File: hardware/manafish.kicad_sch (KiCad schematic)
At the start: 9 parts, among them J12 Magnet, J6 Battery, J8 USB_C_Receptacle_USB2.0_14P

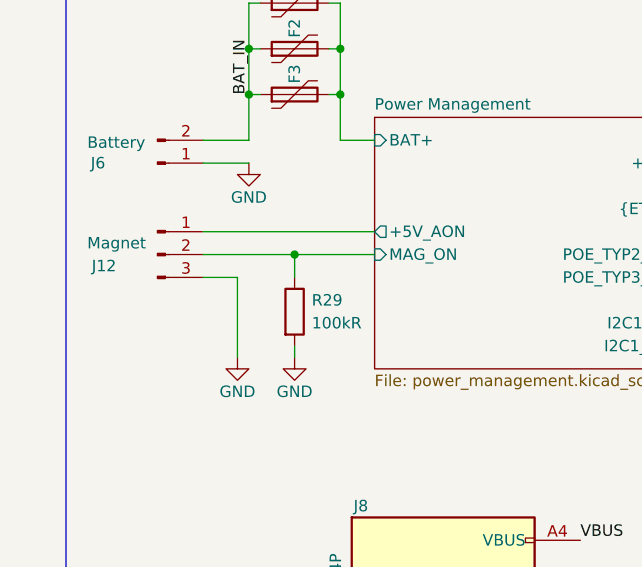
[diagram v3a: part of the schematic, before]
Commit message: Separate the supply pins on breakout headers J9 and J13
Both headers now start with +5V, GND, GND, +3.3V (pins 1-4), so 5 V
and 3.3 V only meet diagonally and each supply pin has GND beside it.
The GPIOs that sat on pins 3/4 moved to the end of each header.

Co-Authored-By: Claude Opus 5.5 <noreply@anthropic.com>
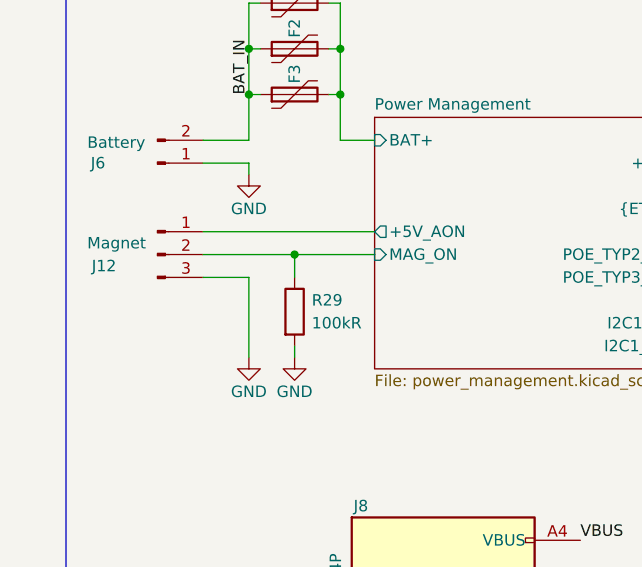
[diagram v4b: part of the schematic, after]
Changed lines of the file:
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@@
 	(wire
 		(pts
+			(xy 35.56 43.18) (xy 35.56 41.91)
+		)
+		(stroke
+			(width 0)
+			(type default)
+		)
+	)
+	(wire
+		(pts
 			(xy 181.61 95.25) (xy 184.15 95.25)
 		)
@@
 		)
 	)
+	(wire
+		(pts
+			(xy 35.56 41.91) (xy 30.48 41.91)
+		)
+		(stroke
+			(width 0)
+			(type default)
+		)
+	)
 	(bus
 		(pts
@@
 	(wire
 		(pts
-			(xy 34.29 54.61) (xy 30.48 54.61)
+			(xy 35.56 54.61) (xy 30.48 54.61)
 		)
 		(stroke
@@
 	(wire
 		(pts
-			(xy 34.29 54.61) (xy 34.29 63.5)
+			(xy 35.56 54.61) (xy 35.56 63.5)
 		)
 		(stroke
@@
 	)
 	(symbol
+		(lib_id "power:GND")
+		(at 35.56 43.18 0)
+		(unit 1)
+		(body_style 1)
+		(exclude_from_sim no)
+		(in_bom no)
+		(on_board no)
+		(in_pos_files no)
+		(dnp no)
+		(property "Reference" "#PWR0175"
+			(at 35.56 49.53 0)
+			(hide yes)
+			(show_name no)
+			(do_not_autoplace no)
+			(effects
+				(font
+					(size 1.27 1.27)
+				)
+			)
+		)
+		(property "Value" "GND"
+			(at 35.56 46.99 0)
+			(show_name no)
+			(do_not_autoplace no)
+			(effects
+				(font
+					(size 1.27 1.27)
+				)
+			)
+		)
+		(property "Footprint" ""
+			(at 35.56 43.18 0)
+			(hide yes)
+			(show_name no)
+			(do_not_autoplace no)
+			(effects
+				(font
+					(size 1.27 1.27)
+				)
+			)
+		)
+		(property "Datasheet" ""
+			(at 35.56 43.18 0)
+			(hide yes)
+			(show_name no)
+			(do_not_autoplace no)
+			(effects
+				(font
+					(size 1.27 1.27)
+				)
+			)
+		)
+		(property "Description" "Power symbol creates a global label with name \"GND\" , ground"
+			(at 35.56 43.18 0)
+			(hide yes)
+			(show_name no)
+			(do_not_autoplace no)
+			(effects
+				(font
+					(size 1.27 1.27)
+				)
+			)
+		)
+		(pin "1"
+		)
+		(instances
+			(project "manafish"
+				(path "/37283e3e-a087-4659-9b29-171eab26a1f6"
+					(reference "#PWR0175")
+					(unit 1)
+				)
+			)
+		)
+	)
+	(symbol
 		(lib_id "Connector:Conn_01x02_Pin")
 		(at 25.4 41.91 0)
@@
 	(symbol
 		(lib_id "power:GND")
-		(at 34.29 63.5 0)
+		(at 35.56 63.5 0)
 		(unit 1)
 		(body_style 1)
@@
 		(dnp no)
 		(property "Reference" "#PWR0170"
-			(at 34.29 69.85 0)
+			(at 35.56 69.85 0)
 			(hide yes)
 			(show_name no)
@@
 		)
 		(property "Value" "GND"
-			(at 34.29 67.31 0)
+			(at 35.56 67.31 0)
 			(show_name no)
 			(do_not_autoplace no)
@@
 		)
 		(property "Footprint" ""
-			(at 34.29 63.5 0)
+			(at 35.56 63.5 0)
 			(hide yes)
 			(show_name no)
@@
 		)
 		(property "Datasheet" ""
-			(at 34.29 63.5 0)
+			(at 35.56 63.5 0)
 			(hide yes)
 			(show_name no)
@@
 		)
 		(property "Description" "Power symbol creates a global label with name \"GND\" , ground"
-			(at 34.29 63.5 0)
+			(at 35.56 63.5 0)
 			(hide yes)
 			(show_name no)
@@
 				)
 			)
-		)
-	)
-	(wire
-		(pts
-			(xy 30.48 41.91) (xy 35.56 41.91)
-		)
-		(stroke
-			(width 0)
-			(type default)
-		)
-	)
-	(symbol
-		(lib_id "power:GND")
-		(at 35.56 41.91 0)
-		(unit 1)
-		(body_style 1)
-		(exclude_from_sim no)
-		(in_bom no)
-		(on_board no)
-		(in_pos_files no)
-		(dnp no)
-		(property "Reference" "#PWR0175"
-			(at 35.56 48.26 0)
-			(hide yes)
-			(show_name no)
-			(do_not_autoplace no)
-			(effects
-				(font
-					(size 1.27 1.27)
-				)
-			)
-		)
-		(property "Value" "GND"
-			(at 35.56 45.72 0)
-			(show_name no)
-			(do_not_autoplace no)
-			(effects
-				(font
-					(size 1.27 1.27)
-				)
-			)
-		)
-		(property "Footprint" ""
-			(at 35.56 41.91 0)
-			(hide yes)
-			(show_name no)
-			(do_not_autoplace no)
-			(effects
-				(font
-					(size 1.27 1.27)
-				)
-			)
-		)
-		(property "Datasheet" ""
-			(at 35.56 41.91 0)
-			(hide yes)
-			(show_name no)
-			(do_not_autoplace no)
-			(effects
-				(font
-					(size 1.27 1.27)
-				)
-			)
-		)
-		(property "Description" "Power symbol creates a global label with name \"GND\" , ground"
-			(at 35.56 41.91 0)
-			(hide yes)
-			(show_name no)
-			(do_not_autoplace no)
-			(effects
-				(font
-					(size 1.27 1.27)
-				)
-			)
-		)
-		(pin "1"
-		)
-		(instances
-			(project "manafish"
-				(path "/37283e3e-a087-4659-9b29-171eab26a1f6"
-					(reference "#PWR0175")
-					(unit 1)
-				)
-			)

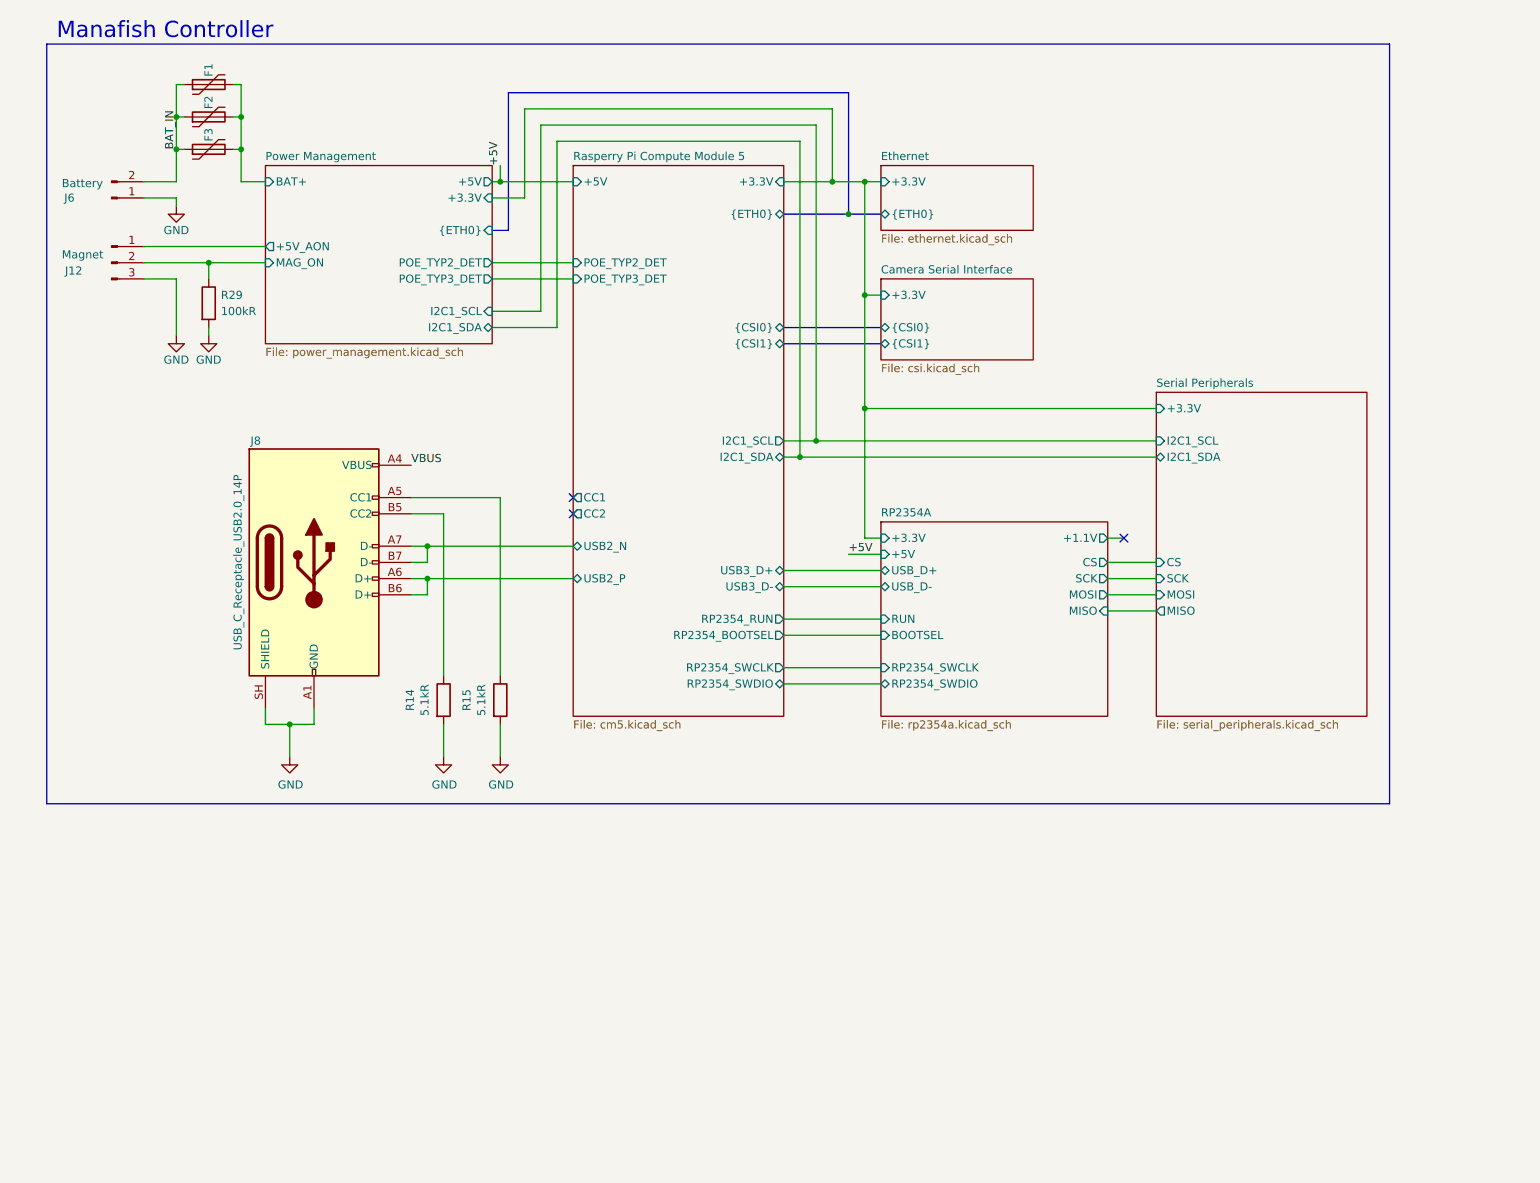
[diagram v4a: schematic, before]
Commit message: Add switchable ESC power, vertical camera connectors and 3.3 V decoupling
- ESC power switch on the root sheet:
  - Battery input J6 changes to XT60PW-M. New XT60PW-F J14 carries switched
    power to both ESCs.
  - Q3 (onsemi NTMFS5C404NLT1G, 40 V, 0.67 mOhm) is driven by the photovoltaic
    driver IC16 (Vishay VOM1271T) from RP2354A GPIO14 (ESC_PWR_EN) via R31.
  - Soft start C46/D6/R32 keeps Q3 in its SOA while the ESC capacitors charge.
    D7 clamps the gate when the battery is unplugged or the thrusters windmill.
  - Static switch with no current limit: the battery BMS protects. Firmware
    timing rules are in the schematic note and the README.
- Camera connectors J5/J11 are now Molex 501951-2230 (vertical, flip lock).
  The footprint numbers pads n = Molex circuit 23-n so a standard Pi 22-pin
  cable lands GND on pin 1, as on the CM5 IO Board.
- Decoupling: 10 uF + 100 nF at the CM5 3.3 V output, 10 uF at each camera
  supply pin.
- Polyfuses F1-F3 removed; the battery feeds the charger path directly.
- New libraries VOM1271T, NTMFS5C404NL, Molex and Vishay, with 3D models.
- PCB updated from the schematic. The layout will be redone.

Co-Authored-By: Claude Opus 5.5 <noreply@anthropic.com>
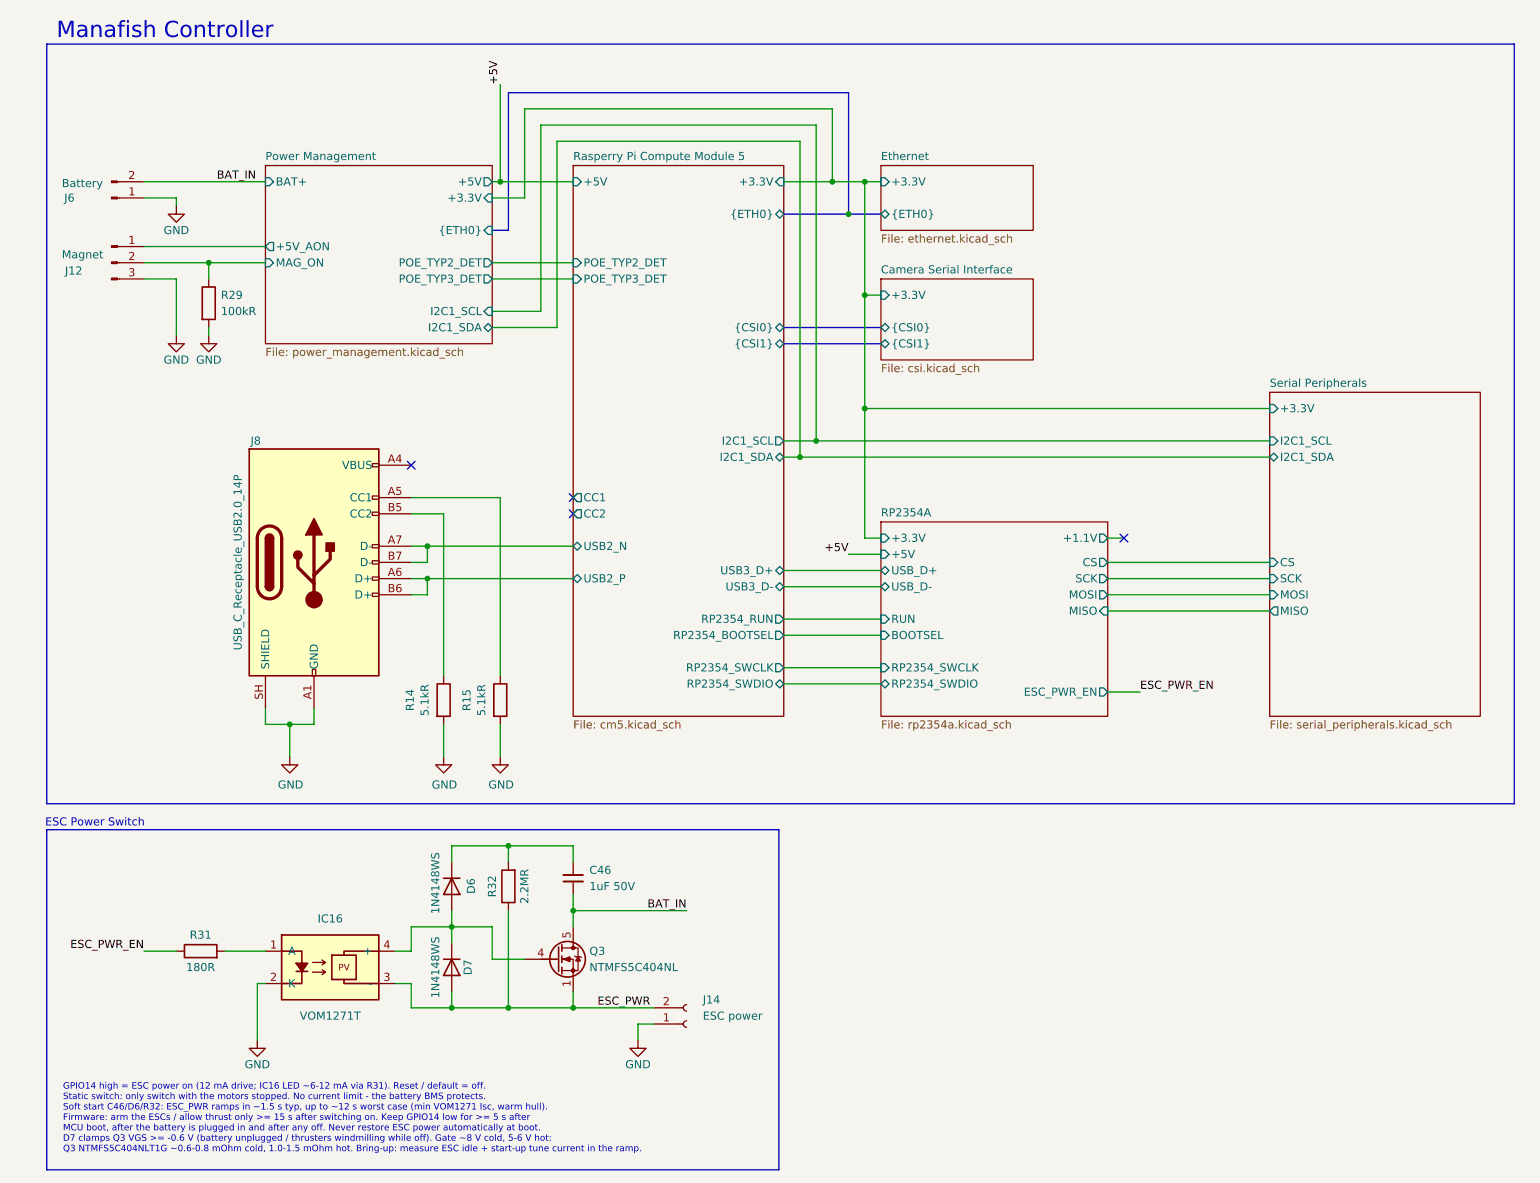
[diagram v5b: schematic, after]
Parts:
- removed F1, F2, F3: MF-LSMF260/33X-2, Fuse:Fuse_2920_7451Metric, symbol Device:Polyfuse
- added C46: 1uF 50V, Capacitor_SMD:C_0603_1608Metric, symbol Device:C_Small
- added D6, D7: 1N4148WS, Diode_SMD:D_SOD-323, symbol Device:D
- added IC16: VOM1271T, Vishay:Vishay_SOP-4_P2.54mm_VOM1271T, symbol VOM1271T:VOM1271T
- added J14: ESC power, Connector_AMASS:AMASS_XT60PW-F_1x02_P7.20mm_Horizontal, symbol Connector:Conn_01x02_Socket
- added Q3: NTMFS5C404NL, Package_SO:ONSemi_SO-8FL_488AA, symbol NTMFS5C404NL:NTMFS5C404NL
- added R31: 180R, Resistor_SMD:R_0402_1005Metric, symbol Device:R
- added R32: 2.2MR, Resistor_SMD:R_0402_1005Metric, symbol Device:R
- J6: footprint Connector_AMASS:AMASS_XT30PW-M_1x02_P2.50mm_Horizontal -> Connector_AMASS:AMASS_XT60PW-M_1x02_P7.20mm_Horizontal; LCSC https://www.lcsc.com/product-detail/C431092.html -> https://www.lcsc.com/product-detail/C98732.html; MPN XT30PW-M30.G.Y -> XT60PW-M; Note Not stocked by Mouser: LCSC C431092 or TME XT30PW-M. -> Not stocked by Mouser: LCSC C98732 or TME XT60PW-M. Mates t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
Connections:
- net BAT_IN: now also C46.2, Q3.5 (D)
- net GND: now also IC16.2 (K), J14.1 (Pin_1)
- net VBUS: no longer names the net of J8.A4 (VBUS), J8.A9 (VBUS), J8.B4 (VBUS), J8.B9 (VBUS)
- new net: IC16.1 (A), R31.2
- new net: D6.2 (A), D7.1 (K), IC16.4 (+), Q3.4 (G)
- new net: C46.1, D6.1 (K), R32.2
- new net ESC_PWR: D7.2 (A), IC16.3 (-), J14.2 (Pin_2), Q3.1 (S), Q3.2 (S), Q3.3 (S), R32.1
- new net ESC_PWR_EN: R31.1
- no-connect marks 3 -> 4
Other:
- sheet RP2354A ports: added ESC_PWR_EN; removed none
- note added: "ESC Power Switch"
- note added: "GPIO14 high = ESC power on (12 mA drive; IC16 LED ~6-12 mA via R31). Reset / default = off. Static switch: only switch with the motors stopped. No current limit - the battery BMS protects. Soft start C46/D6/R32: ESC_PWR ramps in ~1.5 s typ, up to ~12 s worst case (min VOM1271 Isc, warm hull). Firmware: arm the ESCs / allow thrust only >= 15 s after switching on. Keep GPIO14 low for >= 5 s after M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"

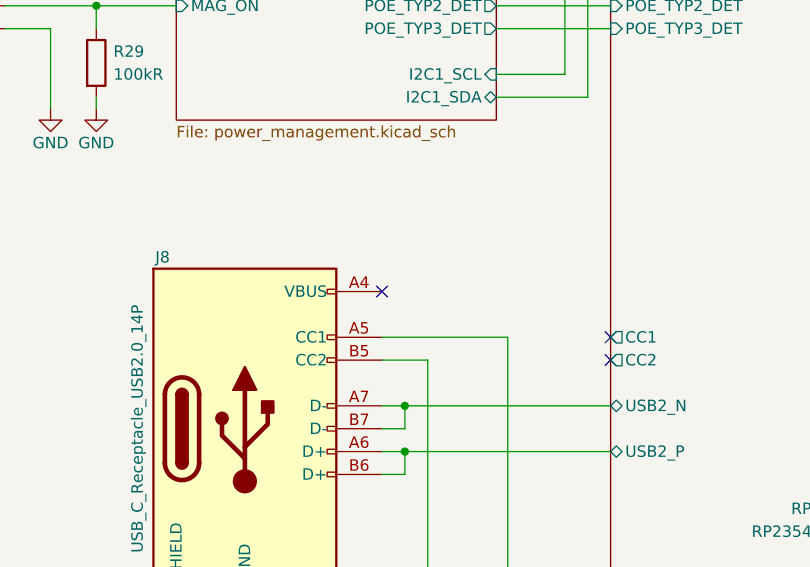
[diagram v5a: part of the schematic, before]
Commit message: Redo the PCB layout (rev 3): 70 x 109.2 mm, connectors on one side, 45° routing
- All connectors on the top: cameras, USB-C and the magnet switch along the
  top edge, the rest at the bottom around the RJ45, which moves towards the
  centre line; C20 near the centre for the tube radius
- Every part except the PoE module IC5 on the top (reflow one side)
- 45-degree routing only, chamfers at least 1.5 x width, traces bundled to
  keep the planes whole
- Small SHT45 tongue with its bypass cap beside it; planes cut out under L2
  with nothing under it; copper 3.4 mm from the CM5 mounting holes
- Charger and RP2354A regulator laid out per their datasheets
- J3/J4 vertical JST GH (BM05B-GHS-TBT); J8 VBUS label restored
- Edge clearance 0.3 mm, netclass patterns follow the current net names,
  hand-soldered THT GND pins get one thermal spoke
- User.Comments fab/assembly notes and README PCB section updated for rev 3

Co-Authored-By: Claude Opus 5.5 <noreply@anthropic.com>
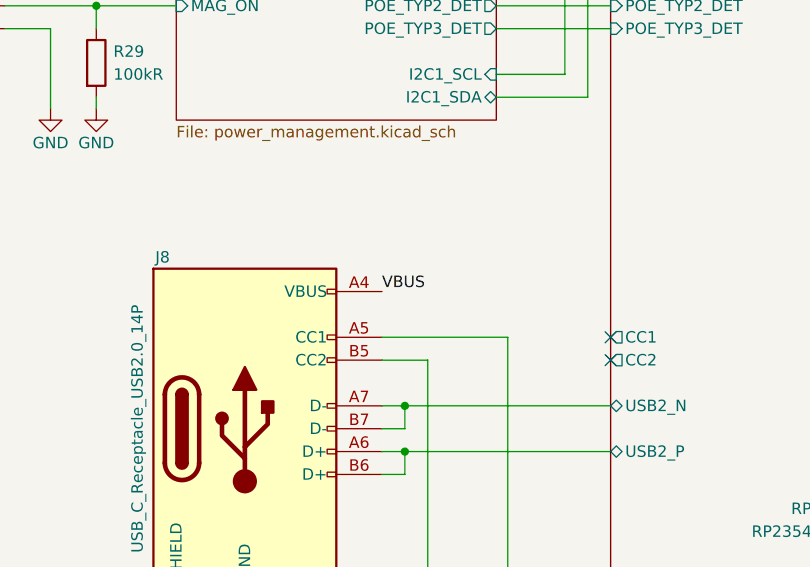
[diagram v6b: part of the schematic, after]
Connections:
- net VBUS: now reaches J8.A4 (VBUS), J8.A9 (VBUS), J8.B4 (VBUS), J8.B9 (VBUS)
- no-connect marks 4 -> 3
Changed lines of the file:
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@@
 		(at 97.79 91.44)
 	)
-	(no_connect
-		(at 72.39 83.82)
+	(label "VBUS"
+		(at 72.39 83.82 0)
+		(effects
+			(font
+				(size 1.27 1.27)
+			)
+			(justify left bottom)
+		)
 	)
 	(wire

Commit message: Add LCSC part numbers and links, fix J7 part number
- Every part found on LCSC gets an "LCSC PN" (C-number) and an "LCSC" product
  link field, in the schematic and on the PCB footprints. Exact matches where
  LCSC lists the part; equivalents with the same specs where it does not or
  has no stock (C46, C26/C28/C30/C33/C34/C40, C29, C31, R6/R7, R21, R24,
  J3/J4, J7/J9/J13). Left empty: IC3, IC5 (not on LCSC), IC10, IC12
  (JLCPCB-only listings).
- J7: the MPN 61301421121 is a 2.54 mm header, but the footprint is 1.27 mm.
  Now Wurth 62201421121 (WR-PHD 1.27 mm 2x7) with matching description,
  datasheet and Mouser fields.
- Interactive HTML BOM in hardware/bom; KiCad project file re-saved.

Co-Authored-By: Claude Opus 5.5 <noreply@anthropic.com>
Claude-Session: https://claude.ai/code/session_01AhLYztcZikG9g81njGtEr1
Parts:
- C46: LCSC (none) -> https://www.lcsc.com/product-detail/C559769.html; LCSC PN (none) -> C559769
- D6, D7: LCSC (none) -> https://www.lcsc.com/product-detail/C60580.html; LCSC PN (none) -> C60580
- IC16: LCSC (none) -> https://www.lcsc.com/product-detail/C146286.html; LCSC PN (none) -> C146286
- J12: LCSC (none) -> https://www.lcsc.com/product-detail/C514175.html; LCSC PN (none) -> C514175
- J14: LCSC PN (none) -> C428722
- J6: LCSC PN (none) -> C98732
- J8: LCSC (none) -> https://www.lcsc.com/product-detail/C3020560.html; LCSC PN (none) -> C3020560
- Q3: LCSC (none) -> https://www.lcsc.com/product-detail/C604432.html; LCSC PN (none) -> C604432
- R14, R15: LCSC (none) -> https://www.lcsc.com/product-detail/C105872.html; LCSC PN (none) -> C105872
- R29: LCSC (none) -> https://www.lcsc.com/product-detail/C60491.html; LCSC PN (none) -> C60491
- R31: LCSC (none) -> https://www.lcsc.com/product-detail/C138045.html; LCSC PN (none) -> C138045
- R32: LCSC (none) -> https://www.lcsc.com/product-detail/C138015.html; LCSC PN (none) -> C138015
